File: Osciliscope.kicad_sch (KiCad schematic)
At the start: 58 parts, among them J2 Conn_01x04_Socket, J3 U.FL, J4 Conn_01x04_Socket, J5 USB_C_Receptacle_USB2.0_14P, J6 Conn_01x02_MountingPin, J7 U.FL, SW1 RotaryEncoder_Switch, SW2 SW_SPST, SW3 SW_Nidec_CAS-120A1, SW4 SW_Nidec_CAS-120A1, SW5 RotaryEncoder_Switch, SW6 RotaryEncoder_Switch, U1 MCP1700x-330xxMB, U2 ADC082S101, U3 IP2721, U4 AZ1084-5.0, U5 TLV9061xDBV, U7 TLV9061xDBV, U8 MCP4251-104E/ML-ND

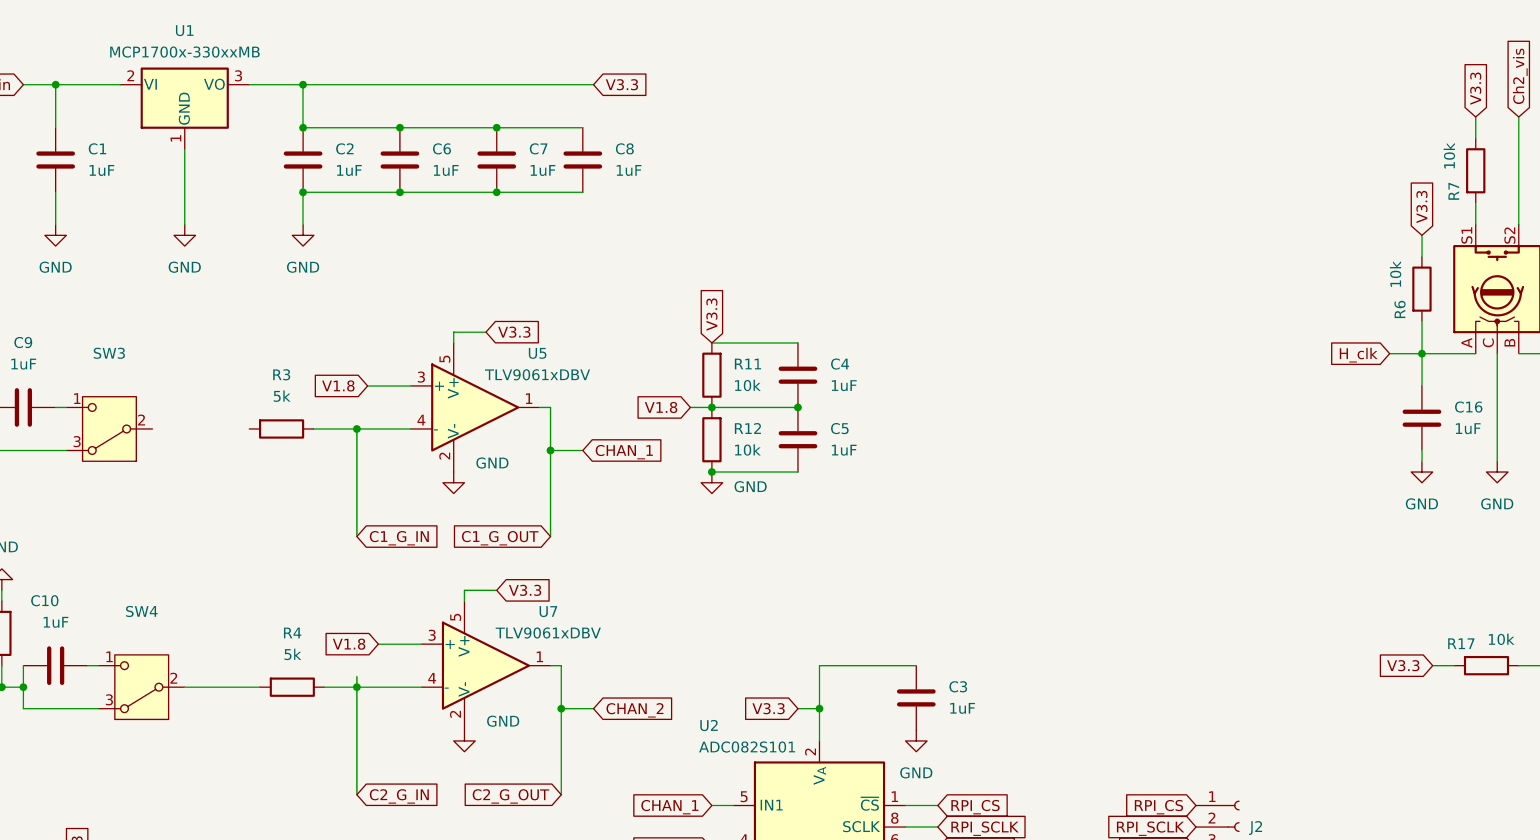
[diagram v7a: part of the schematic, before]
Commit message: sockets for connectors
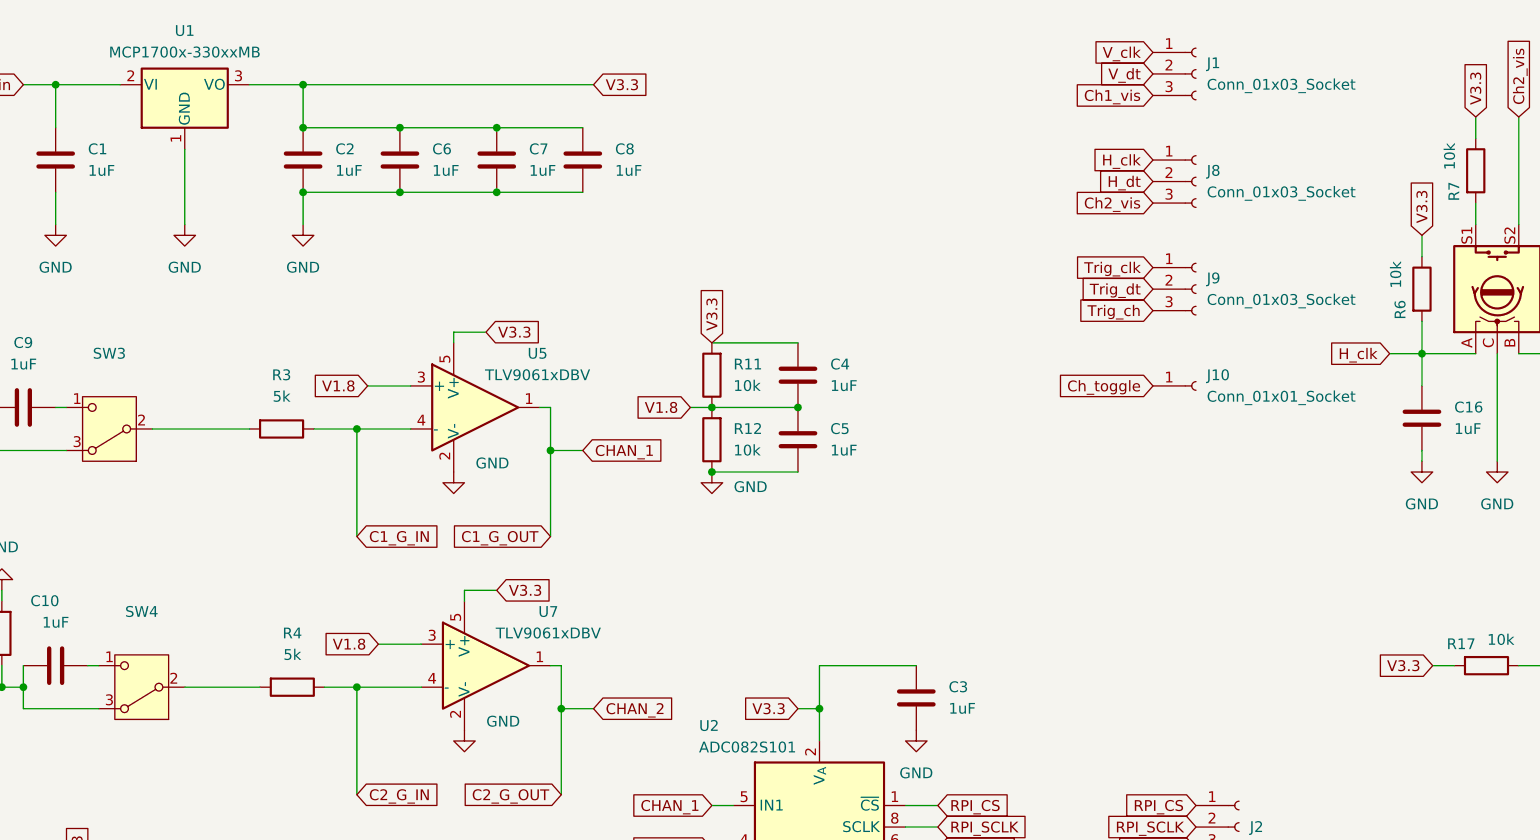
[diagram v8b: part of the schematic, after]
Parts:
- added J1, J8, J9: Conn_01x03_Socket, symbol Connector:Conn_01x03_Socket
- added J10: Conn_01x01_Socket, symbol Connector:Conn_01x01_Socket
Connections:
- net Ch1_vis: now also J1.3 (Pin_3)
- net Ch2_vis: now also J8.3 (Pin_3)
- net Ch_toggle: now also J10.1 (Pin_1)
- net H_clk: now also J8.1 (Pin_1)
- net H_dt: now also J8.2 (Pin_2)
- net Trig_ch: now also J9.3 (Pin_3)
- net Trig_clk: now also J9.1 (Pin_1)
- net Trig_dt: now also J9.2 (Pin_2)
- net V_clk: now also J1.1 (Pin_1)
- net V_dt: now also J1.2 (Pin_2)
- net at R3.2: now also SW3.2 (B)
